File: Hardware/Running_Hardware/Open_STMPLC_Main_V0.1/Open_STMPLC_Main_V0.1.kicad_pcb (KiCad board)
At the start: 2 copper layers, 168.8 x 90 mm, 148 parts, among them J1 Conn_02x08_Odd_Even, J10 10144518-041802LF, J11 HY951180A, J2 USB C, J4 TF-01A, J5 Conn_Coaxial, J6 Conn_Coaxial, J7 Simcard_Nano, J8 10144518-041802LF, J9 10144518-041802LF, Q1 DTC143Z, Q2 DTC143Z, Q3 DTC143Z, Q4 DTC143Z, Q5 DTC143Z, Q6 DTC143Z, Q7 DTC143Z, SW1 Switch, SW2 SW_SPDT, SW3 Switch_6x6, U1 STM32F407IGTx, U2 ADM2587E, U3 TPS3430WDRC, U4 CH340C, U5 AP63203WU, U6 W25Q64JVSSIQ, U7 LAN8720A, U8 EC200U, Y1 48MHz, Y2 32.768kHz, Y3 25MHz

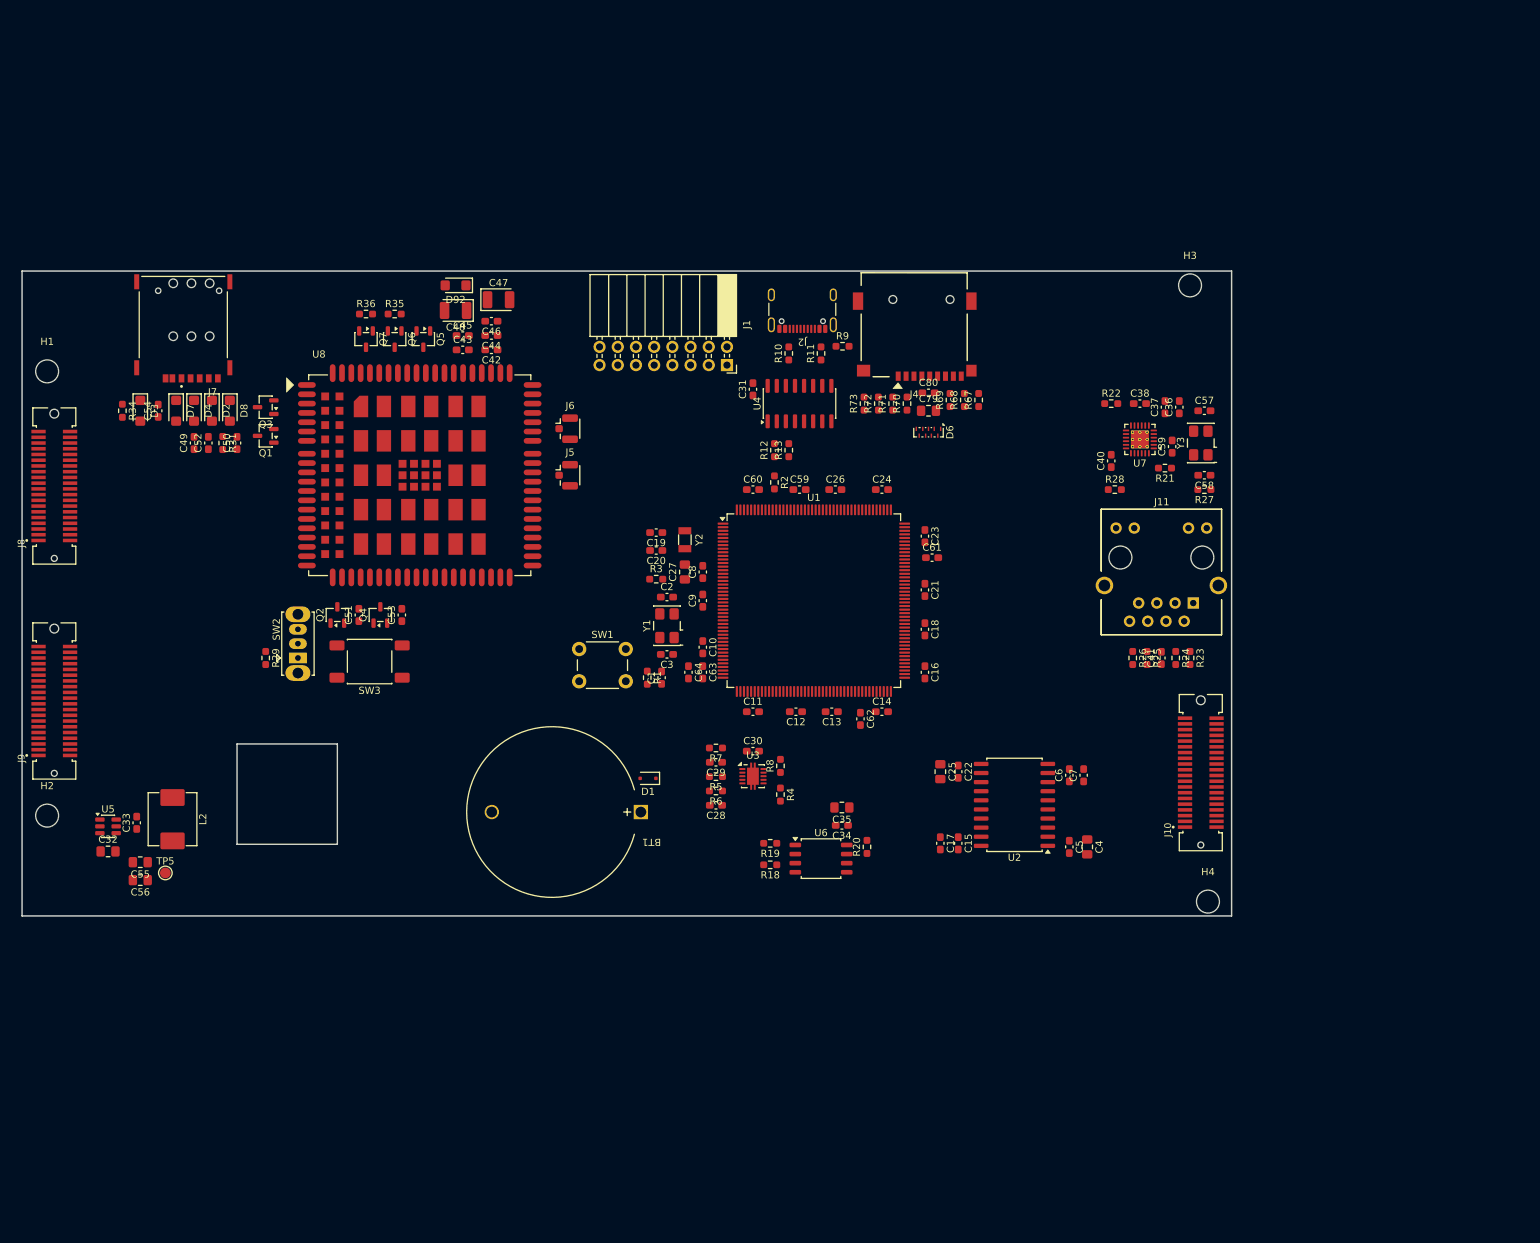
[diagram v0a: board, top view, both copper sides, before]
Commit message: Schematic updates
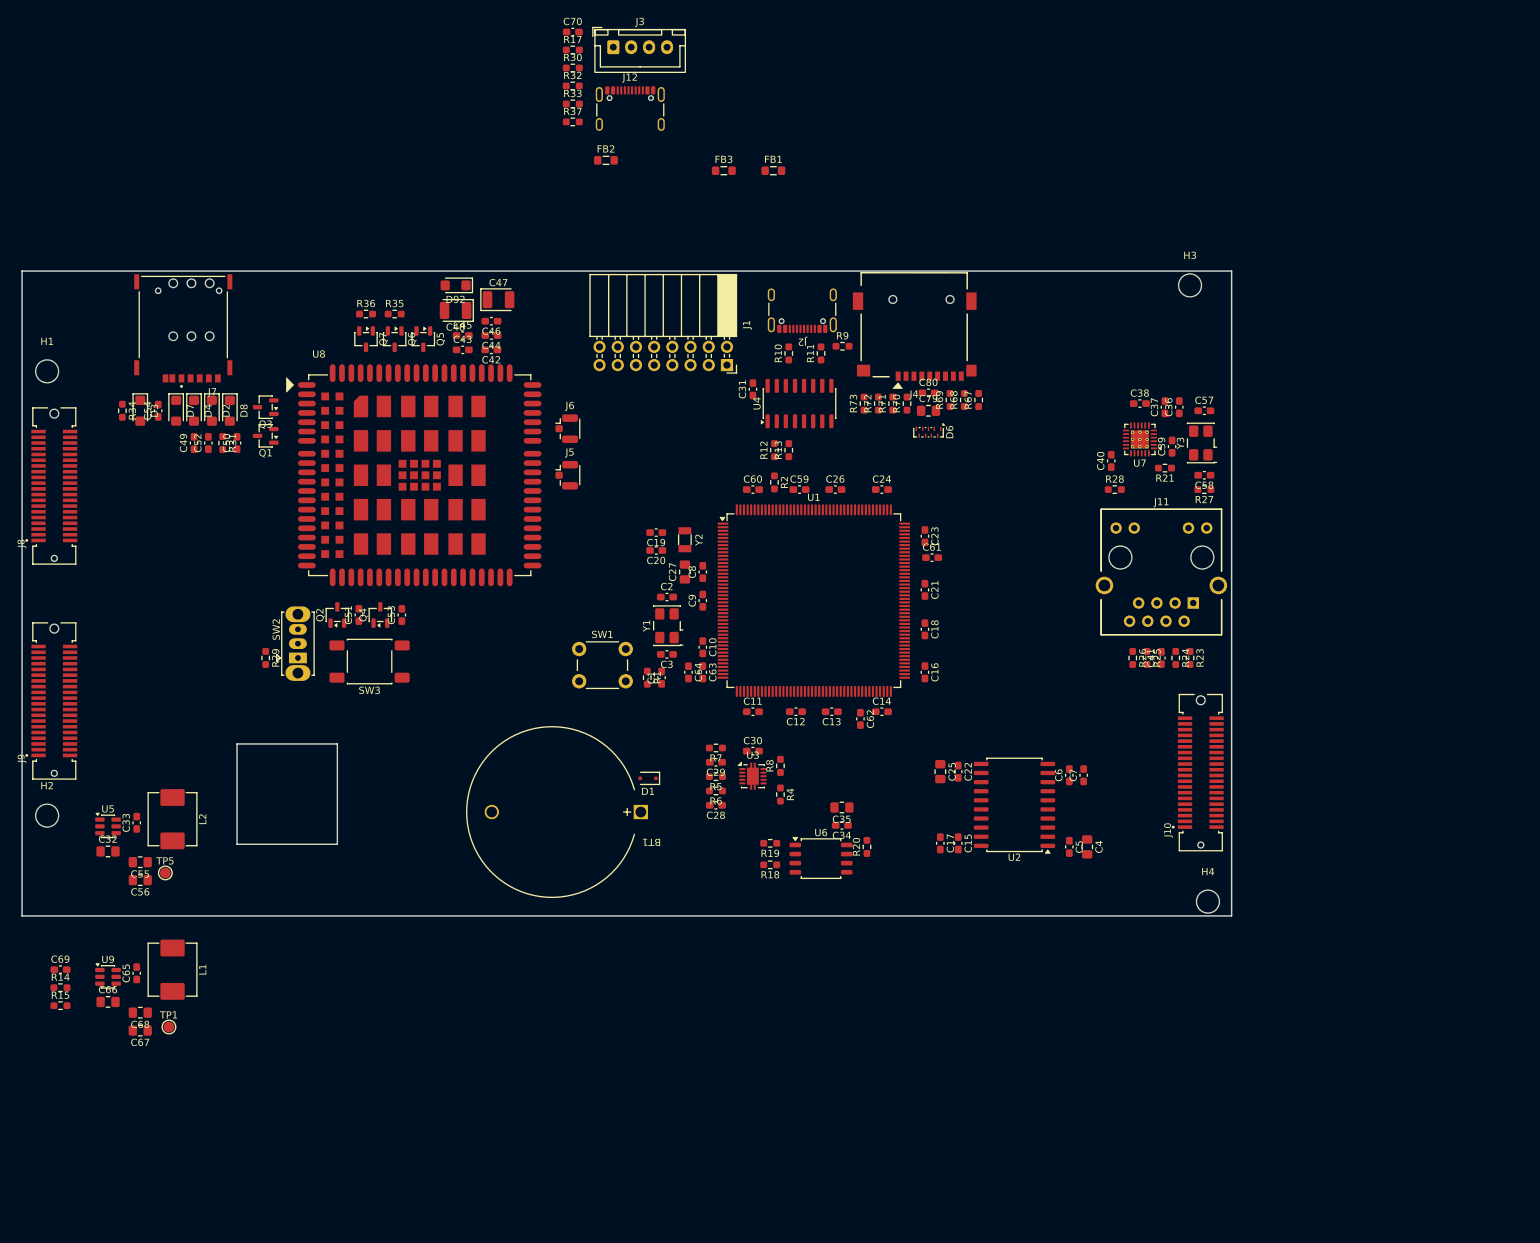
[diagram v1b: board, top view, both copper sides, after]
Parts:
- removed R22, R3: 0R, Resistor_SMD:R_0603_1608Metric_Pad0.98x0.95mm_HandSolder
- added C65: 100nF, Capacitor_SMD:C_0603_1608Metric_Pad1.08x0.95mm_HandSolder, F.Cu at (66.0, 148.0)
- added C66: 10uF, Capacitor_SMD:C_0805_2012Metric_Pad1.18x1.45mm_HandSolder, F.Cu at (62.0, 152.0)
- added C67: 22uF, Capacitor_SMD:C_0805_2012Metric_Pad1.18x1.45mm_HandSolder, F.Cu at (66.5, 156.0)
- added C68: 22uF, Capacitor_SMD:C_0805_2012Metric_Pad1.18x1.45mm_HandSolder, F.Cu at (66.5, 153.5)
- added C69: 100pF, Capacitor_SMD:C_0603_1608Metric_Pad1.08x0.95mm_HandSolder, F.Cu at (55.4, 147.5)
- added C70: 100nF, Capacitor_SMD:C_0603_1608Metric_Pad1.08x0.95mm_HandSolder, F.Cu at (126.9, 16.6)
- added FB1: BLM21PG121SN1D, Inductor_SMD:L_0805_2012Metric_Pad1.05x1.20mm_HandSolder, F.Cu at (154.8, 36.0)
- added FB2: BLM21PG121SN1D, Inductor_SMD:L_0805_2012Metric_Pad1.05x1.20mm_HandSolder, F.Cu at (131.5, 34.5)
- added FB3: BLM21PG121SN1D, Inductor_SMD:L_0805_2012Metric_Pad1.05x1.20mm_HandSolder, F.Cu at (147.9, 36.0)
- added J12: USB C, Connector_USB:USB_C_Receptacle_GCT_USB4105-xx-A_16P_TopMnt_Horizontal, F.Cu at (134.9, 28.5)
- added J3: Conn_01x04, Connector_JST:JST_XH_B4B-XH-A_1x04_P2.50mm_Vertical, F.Cu at (132.5, 18.8)
- added L1: 3.3uH, Inductor_SMD:L_Abracon_ASPI-0630LR, F.Cu at (71.0, 147.5)
- added R14: 68K, Resistor_SMD:R_0603_1608Metric_Pad0.98x0.95mm_HandSolder, F.Cu at (55.4, 150.0)
- added R15: 18K, Resistor_SMD:R_0603_1608Metric_Pad0.98x0.95mm_HandSolder, F.Cu at (55.4, 152.5)
- added R17: 10K, Resistor_SMD:R_0603_1608Metric_Pad0.98x0.95mm_HandSolder, F.Cu at (126.9, 19.1)
- added R30: 10K, Resistor_SMD:R_0603_1608Metric_Pad0.98x0.95mm_HandSolder, F.Cu at (126.9, 21.7)
- added R32: 0R, Resistor_SMD:R_0603_1608Metric_Pad0.98x0.95mm_HandSolder, F.Cu at (126.9, 24.2)
- added R33: 5.1K, Resistor_SMD:R_0603_1608Metric_Pad0.98x0.95mm_HandSolder, F.Cu at (126.9, 26.7)
- added R37: 5.1K, Resistor_SMD:R_0603_1608Metric_Pad0.98x0.95mm_HandSolder, F.Cu at (126.9, 29.2)
- added TP1: TestPoint, TestPoint:TestPoint_Pad_D1.5mm, F.Cu at (70.5, 155.5)
- added U9: AP63200WU, Package_TO_SOT_SMD:TSOT-23-6, F.Cu at (62.0, 148.5)
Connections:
- net +3V8 renamed Net-(D92-A1)
- net /Microcontroller/STM_DN renamed /Microcontroller/DEBUG_DN
- net /Microcontroller/STM_DP renamed /Microcontroller/DEBUG_DP

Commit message: Component placement main pcb
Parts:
- added C71: 10uF, Capacitor_SMD:C_0805_2012Metric_Pad1.18x1.45mm_HandSolder, F.Cu at (81.0, 112.5)
- added C72: 10uF, Capacitor_SMD:C_0805_2012Metric_Pad1.18x1.45mm_HandSolder, F.Cu at (85.5, 112.5)
- added R3: 0R, Resistor_SMD:R_0603_1608Metric_Pad0.98x0.95mm_HandSolder, F.Cu at (117.5, 127.0)
- added U10: AP63205WU, Package_TO_SOT_SMD:TSOT-23-6, F.Cu at (66.5, 132.5)
- BT1: moved to B.Cu
- J3: footprint Connector_JST:JST_XH_B4B-XH-A_1x04_P2.50mm_Vertical -> Connector_PinHeader_2.54mm:PinHeader_1x04_P2.54mm_Horizontal
- SW1: value Switch -> Switch_6x6; footprint Button_Switch_THT:SW_PUSH_6mm_H5mm -> Button_Switch_SMD:SW_Push_1P1T_NO_E-Switch_TL3301NxxxxxG
- SW2: footprint Button_Switch_THT:SW_Slide_SPDT_Straight_CK_OS102011MS2Q -> Button_Switch_SMD:SW_SPDT_PCM12
- U5: value AP63203WU -> AMS1117-3.3; footprint Package_TO_SOT_SMD:TSOT-23-6 -> Package_TO_SOT_SMD:SOT-223-3_TabPin2
- moved FB1 98.0 mm to (60.6, 63.0), turned to -90 degrees
- moved C70 86.3 mm to (199.0, 64.0)
- moved R17 82.1 mm to (195.0, 65.0), turned to -90 degrees
- moved R30 78.7 mm to (192.5, 65.0), turned to -90 degrees
- moved J3 73.5 mm to (192.7, 60.9), turned to 90 degrees
- moved FB3 65.4 mm to (206.0, 66.0)
- moved FB2 59.4 mm to (146.5, 92.0), turned to 180 degrees
- moved R32 56.7 mm to (169.5, 61.5), turned to -90 degrees
- moved SW2 54.7 mm to (67.5, 53.5), turned to 180 degrees
- moved TP1 53.6 mm to (73.5, 102.0), turned to 90 degrees
- moved C47 53.2 mm to (64.1, 63.0), turned to 90 degrees
- moved C34 52.2 mm to (114.5, 112.0)
- moved C35 52.2 mm to (114.5, 109.5)
- moved R18 52.2 mm to (104.5, 117.5)
- moved R19 52.2 mm to (104.5, 114.5)
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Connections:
- net /Microcontroller/SD_MISO renamed /Microcontroller/Flash_MISO
- net /Microcontroller/SD_MOSI renamed /Microcontroller/Flash_MOSI
- net /Storage/SD_DET renamed /SD_DET
- C1 pad 1: /Microcontroller/~{WDO} -> /Microcontroller/~{STM_RST}
- C33 pad 1: Net-(U5-SW) -> Net-(U10-SW)
- C33 pad 2: Net-(U5-BST) -> Net-(U10-BST)
- C55 pad 1: +3V3 -> +5V
- C56 pad 1: +3V3 -> +5V
- D6 pad 1: /Storage/SD_DAT1 -> /SD_DAT1
- D6 pad 2: /Storage/SD_DAT0 -> /SD_DAT0
- D6 pad 4: /Storage/SD_CMD -> /SD_CMD
- D6 pad 5: /Storage/SD_DAT3 -> /SD_DAT3
- D6 pad 6: /Storage/SD_DAT2 -> /SD_DAT2
- D6 pad 8: /Storage/SD_CLK -> /SD_CLK
- J3 pad 1: +3V3 -> /Microcontroller/DISP_SDA
- J3 pad 2: GND -> /Microcontroller/DISP_SCL
- J3 pad 3: /Microcontroller/DISP_SCL -> GND
- J3 pad 4: /Microcontroller/DISP_SDA -> +3V3
- J4 pad 1: /Storage/SD_DAT2 -> /SD_DAT2
- J4 pad 2: /Storage/SD_DAT3 -> /SD_DAT3
- J4 pad 3: /Storage/SD_CMD -> /SD_CMD
- J4 pad 5: /Storage/SD_CLK -> /SD_CLK
- J4 pad 7: /Storage/SD_DAT0 -> /SD_DAT0
- J4 pad 8: /Storage/SD_DAT1 -> /SD_DAT1
- L2 pad 1: Net-(U5-SW) -> Net-(U10-SW)
- L2 pad 2: +3V3 -> +5V
- R1 pad 2: /Microcontroller/~{WDO} -> /Microcontroller/~{STM_RST}
- R68 pad 2: /Storage/SD_DAT1 -> /SD_DAT1
- R69 pad 2: /Storage/SD_DAT0 -> /SD_DAT0
- R70 pad 2: /Storage/SD_CLK -> /SD_CLK
- R71 pad 2: /Storage/SD_CMD -> /SD_CMD
- R72 pad 2: /Storage/SD_DAT3 -> /SD_DAT3
- R73 pad 2: /Storage/SD_DAT2 -> /SD_DAT2
- SW1 pad 2: /Microcontroller/~{WDO} -> /Microcontroller/~{STM_RST}
- TP5 pad 1: +3V3 -> +5V
- U1 pad 117: unconnected-(U1-PC8-Pad117) -> /SD_DAT0
- U1 pad 118: unconnected-(U1-PC9-Pad118) -> /SD_DAT1
- U1 pad 139: unconnected-(U1-PC10-Pad139) -> /SD_DAT2
- U1 pad 140: unconnected-(U1-PC11-Pad140) -> /SD_DAT3
- U1 pad 141: unconnected-(U1-PC12-Pad141) -> /SD_CLK
- U1 pad 144: unconnected-(U1-PD2-Pad144) -> /SD_CMD
- U1 pad 154: unconnected-(U1-PG11-Pad154) -> /Ethernet/ETH_TXEN
- U1 pad 156: unconnected-(U1-PG13-Pad156) -> /Ethernet/ETH_TXD0
- U1 pad 157: unconnected-(U1-PG14-Pad157) -> /Ethernet/ETH_TXD1
- U1 pad 31: /Microcontroller/~{WDO} -> /Microcontroller/~{STM_RST}
- U1 pad 33: unconnected-(U1-PC1-Pad33) -> /Ethernet/ETH_MDC
- U1 pad 41: unconnected-(U1-PA1-Pad41) -> /Ethernet/ETH_REFCLKO
- U1 pad 42: unconnected-(U1-PA2-Pad42) -> /Ethernet/ETH_MDIO
- U1 pad 53: unconnected-(U1-PA7-Pad53) -> /Ethernet/ETH_CRSDV
- U1 pad 54: unconnected-(U1-PC4-Pad54) -> /Ethernet/ETH_RXD0
- U1 pad 55: unconnected-(U1-PC5-Pad55) -> /Ethernet/ETH_RXD1
- U5 pad 1: +3V3 -> GND
- U5 pad 2: +24V -> +3V3
- U5 pad 3: +24V -> +5V
- U6 pad 6: /Storage/SD_CLK -> /Microcontroller/Flash_CLK
- U7 pad 14: /Ethernet/ETH_~{INT} -> /Ethernet/ETH_REFCLKO

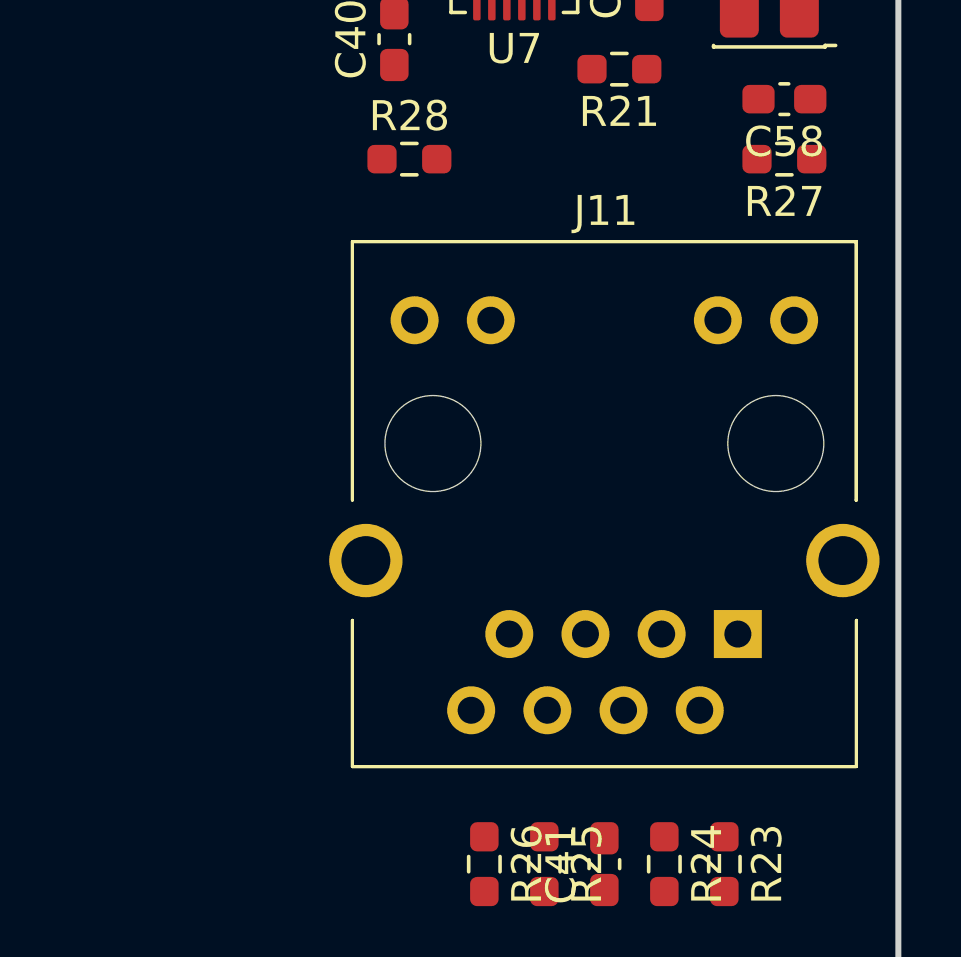
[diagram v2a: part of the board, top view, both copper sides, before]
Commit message: IO board layout completion and DRC clear
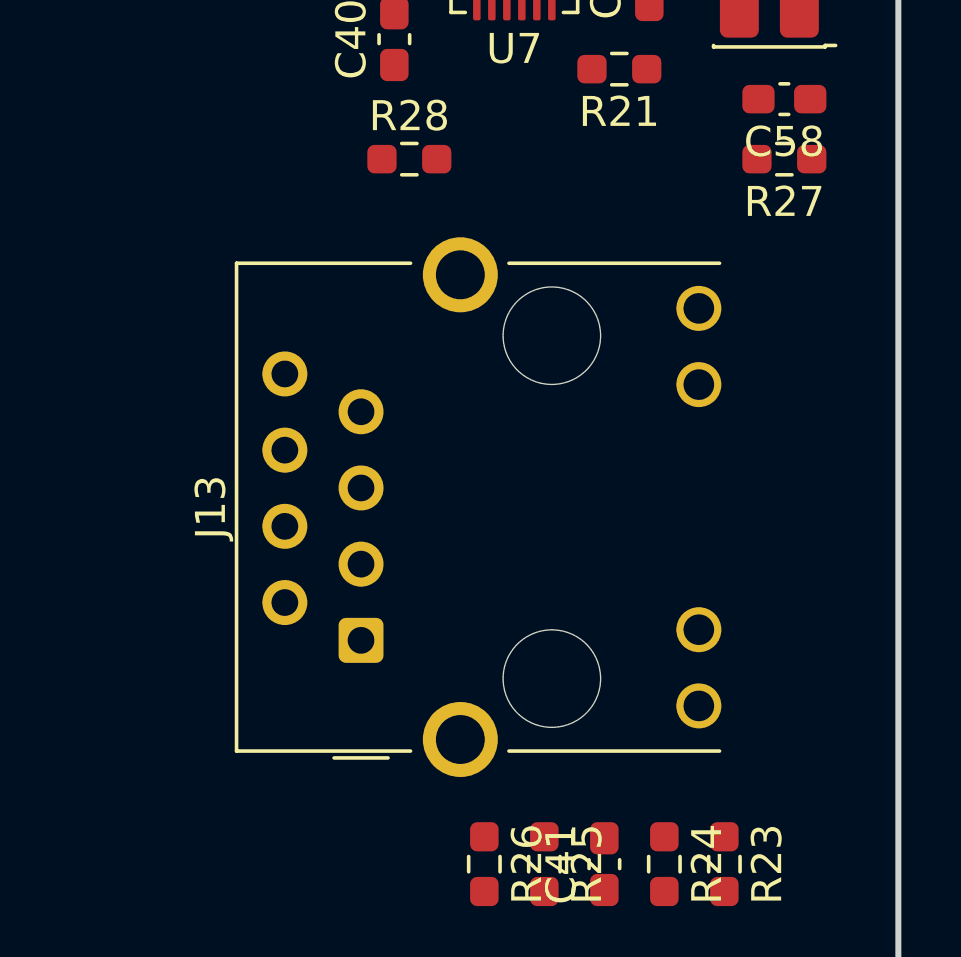
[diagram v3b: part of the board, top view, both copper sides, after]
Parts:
- removed J11: HY951180A, HY951180A:HY951180A
- added J13: RJ45_Hanrun_HR911105A_Horizontal, Connector_RJ:RJ45_Hanrun_HR911105A_Horizontal, F.Cu at (200.9, 96.5)
